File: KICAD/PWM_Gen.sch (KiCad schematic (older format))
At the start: 17 parts, among them U1 AD8030, U13 AD8030

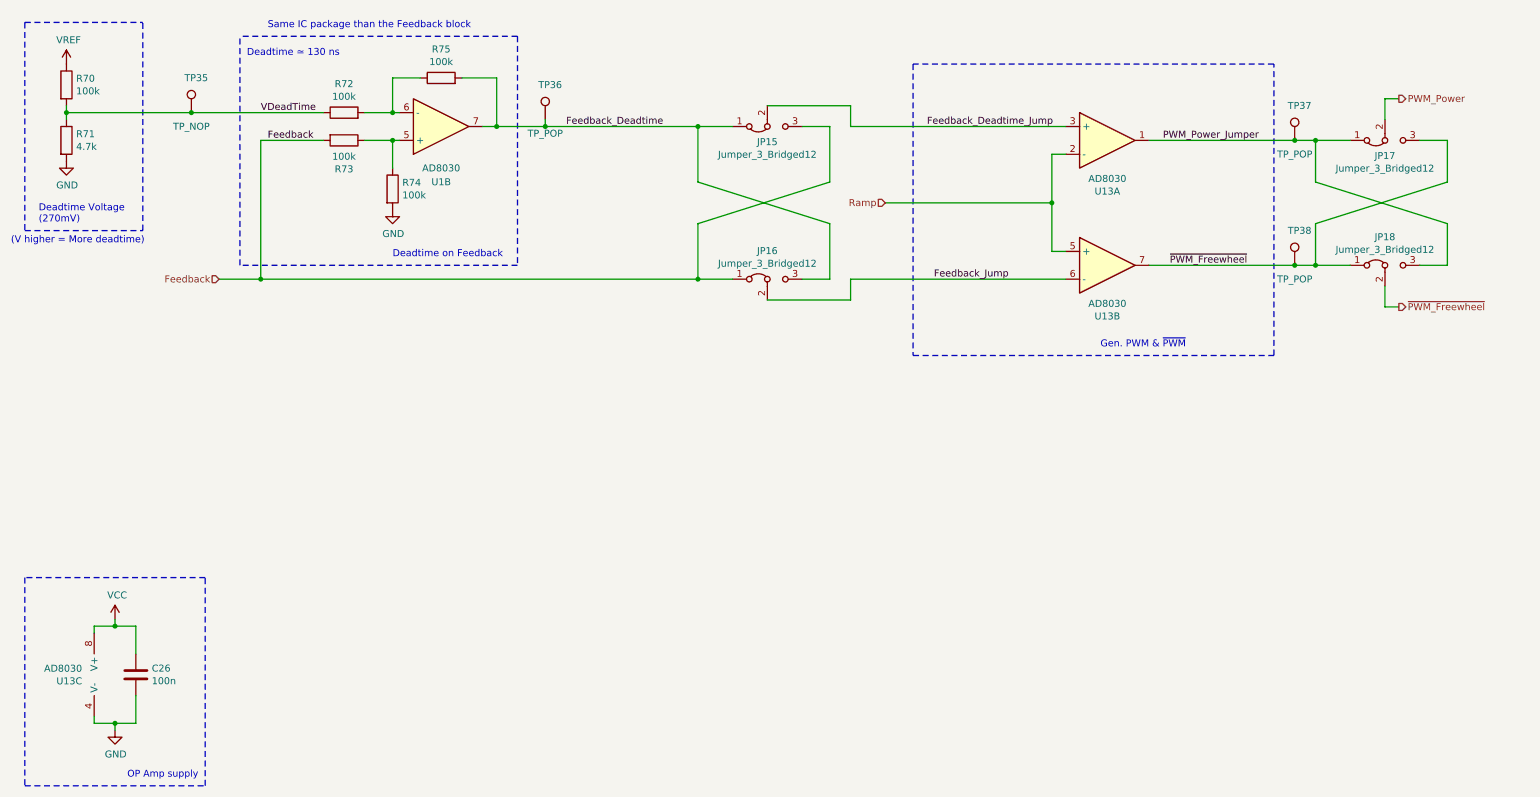
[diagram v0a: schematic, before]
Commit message: fixed a mistake w/ not connected net and net naming mistake
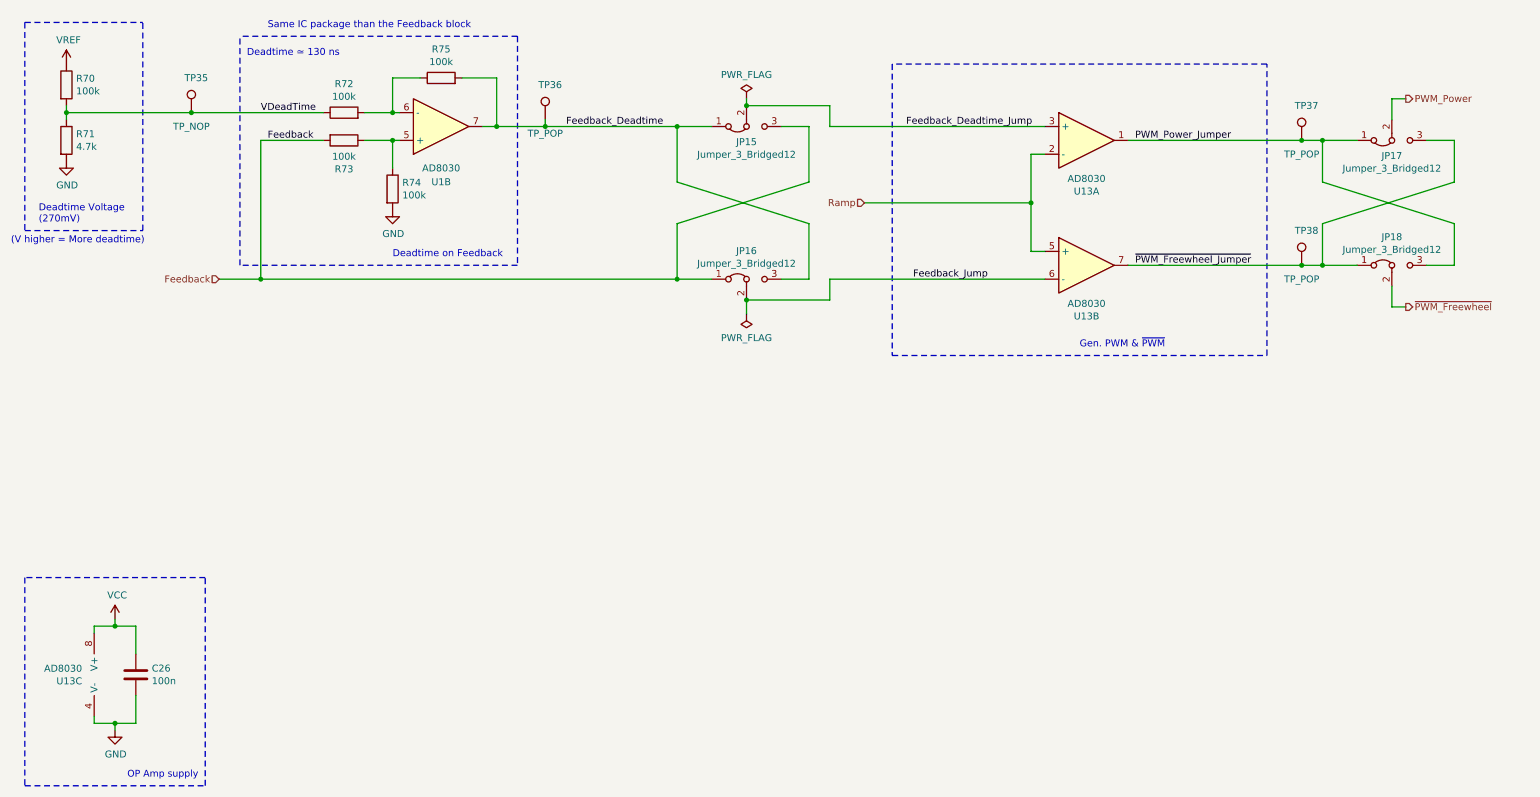
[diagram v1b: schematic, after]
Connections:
- net ~PWM_Freewheel: no longer JP17.3 (B), JP18.1 (A), TP38.1, U13.7
- new net ~PWM_Freewheel_Jumper: JP17.3 (B), JP18.1 (A), TP38.1, U13.7
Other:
- moved on the sheet: JP15, JP16, JP17, JP18, TP37, TP38, U13A, U13B

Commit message: V1.0 of the schematic
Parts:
- U1, U13: footprint Package_SO:SO-8_5.3x6.2mm_P1.27mm -> Sesame_footprint:SO-8_5.3x6.2mm_P1.27mm
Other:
- note added: "Gen. PWM_Power & ~PWM_Freewheel"
- note added: "Same IC package as the Feedback block"
- note removed: "Gen. PWM & ~PWM"
- note removed: "Same IC package than the Feedback block"
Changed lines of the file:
@@
 Sheet 13 17
 Title "SESAME"
-Date ""
-Rev ""
+Date "2021-09-23"
+Rev "1"
 Comp "ALEEA"
 Comment1 "Dessin : Kevin & Sarah & Guillaume Arthaud"
@@
 Wire Notes Line
 	550  2200 1400 2200
-Text Notes 450  3800 0    50   ~ 0
+Text Notes 500  3800 0    50   ~ 0
 (V higher = More deadtime)
 Wire Wire Line
@@
 	7800 3500 7800 3850
 Connection ~ 7800 3500
-Text Notes 8150 4550 0    50   ~ 0
-Gen. PWM & ~PWM
+Text Notes 8100 4550 0    50   ~ 0
+Gen. PWM_Power & ~PWM_Freewheel
 Wire Wire Line
 	10150 3950 9900 3950
@@
 	1950 4050 2250 4050
 Text Notes 2300 2250 0    50   ~ 0
-Same IC package than the Feedback block
+Same IC package as the Feedback block
 $Comp
 L Sesame:AD8030 U1
@@
 F 0 "U1" H 3550 3350 50  0000 C CNN
 F 1 "AD8030" H 3550 3250 50  0000 C CNN
-F 2 "Package_SO:SO-8_5.3x6.2mm_P1.27mm" H 3550 2950 50  0001 C CNN
+F 2 "Sesame_footprint:SO-8_5.3x6.2mm_P1.27mm" H 3550 2950 50  0001 C CNN
 F 3 "~" H 3550 2950 50  0001 C CNN
 	2    3550 2950
@@
 F 0 "U13" H 963 6854 50  0000 R CNN
 F 1 "AD8030" H 963 6945 50  0000 R CNN
-F 2 "Package_SO:SO-8_5.3x6.2mm_P1.27mm" H 1150 6900 50  0001 C CNN
+F 2 "Sesame_footprint:SO-8_5.3x6.2mm_P1.27mm" H 1150 6900 50  0001 C CNN
 F 3 "~" H 1150 6900 50  0001 C CNN
 	3    1150 6900
@@
 F 0 "U13" H 8200 3583 50  0000 C CNN
 F 1 "AD8030" H 8200 3674 50  0000 C CNN
-F 2 "Package_SO:SO-8_5.3x6.2mm_P1.27mm" H 8200 3950 50  0001 C CNN
+F 2 "Sesame_footprint:SO-8_5.3x6.2mm_P1.27mm" H 8200 3950 50  0001 C CNN
 F 3 "~" H 8200 3950 50  0001 C CNN
 	2    8200 3950
@@
 F 0 "U13" H 8200 2683 50  0000 C CNN
 F 1 "AD8030" H 8200 2774 50  0000 C CNN
-F 2 "Package_SO:SO-8_5.3x6.2mm_P1.27mm" H 8200 3050 50  0001 C CNN
+F 2 "Sesame_footprint:SO-8_5.3x6.2mm_P1.27mm" H 8200 3050 50  0001 C CNN
 F 3 "~" H 8200 3050 50  0001 C CNN
 	1    8200 3050

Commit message: added gitignore and docs need cleenup
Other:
- note added: "TS3702\nComp push-pull"
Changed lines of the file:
@@
 	5750 4200 5750 4300
 Connection ~ 5750 4200
+Text Notes 7850 2450 0    100  ~ 0
+TS3702\nComp push-pull
 $EndSCHEMATC
